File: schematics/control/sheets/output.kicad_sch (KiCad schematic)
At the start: 17 parts, among them U13 NE5532, U14 TL072

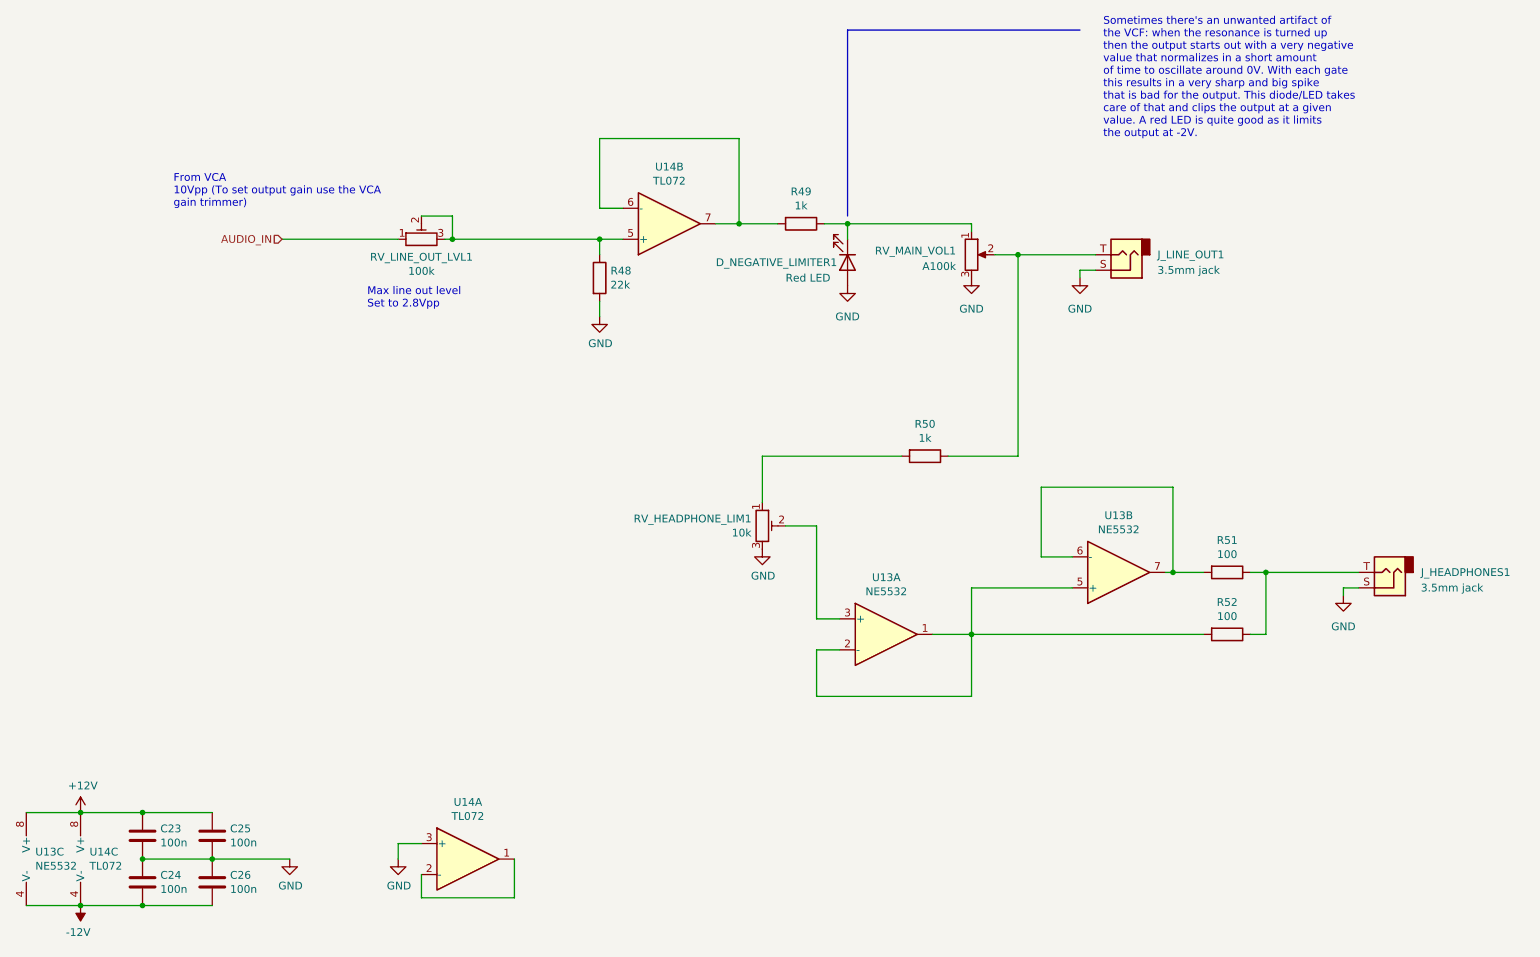
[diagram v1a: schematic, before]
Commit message: Added pulse width mod schematics
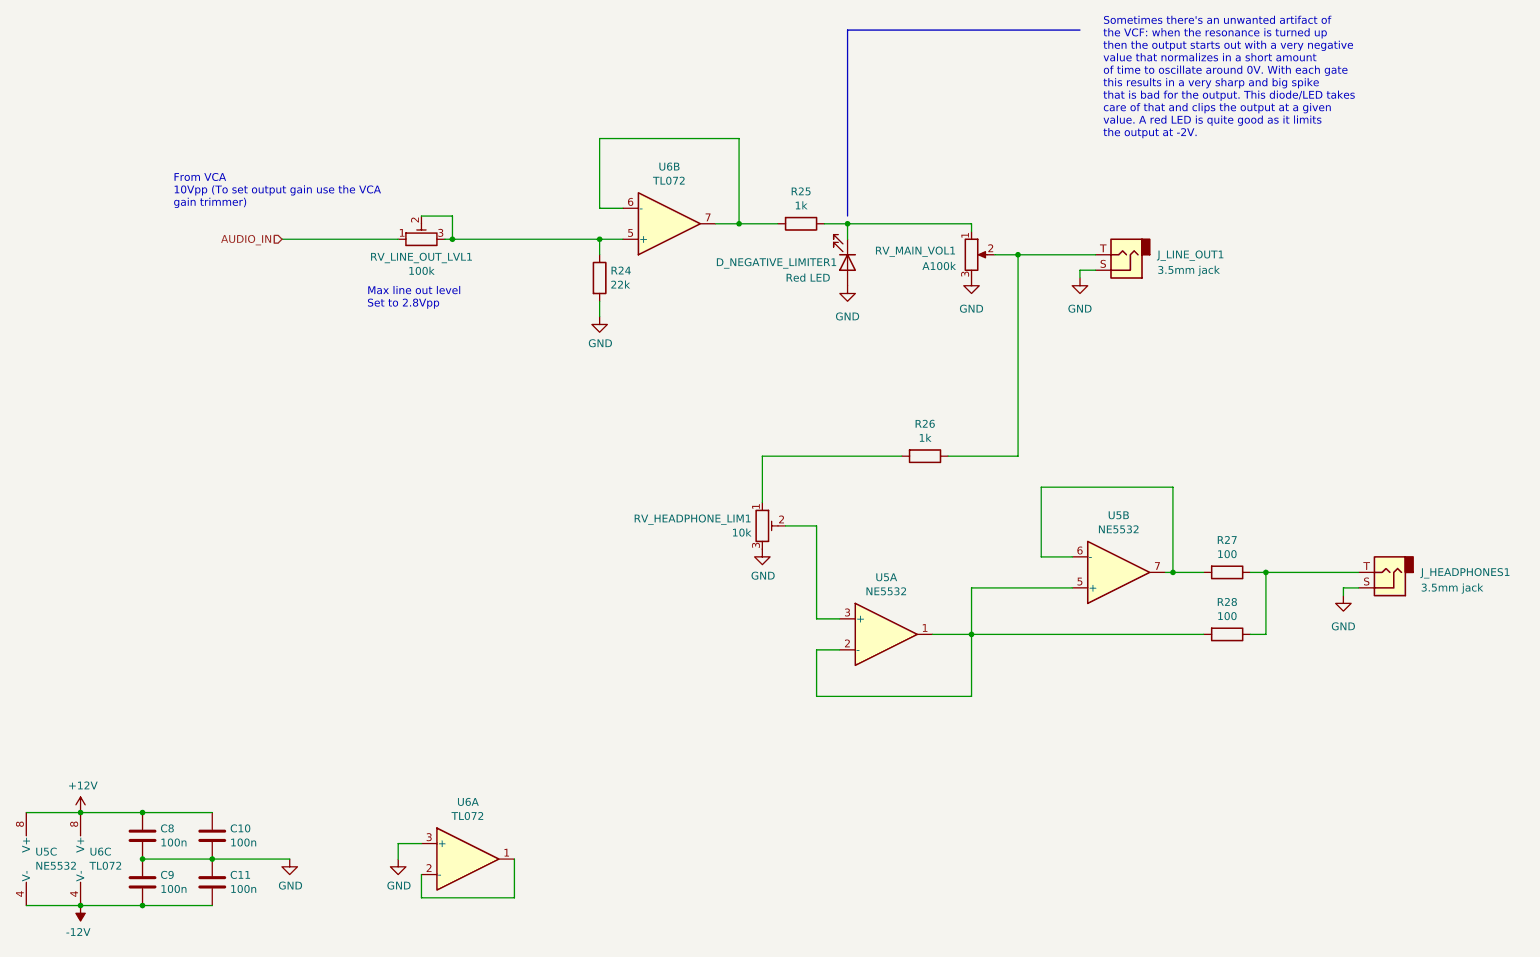
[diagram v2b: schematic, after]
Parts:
- renumbered C25 to C10, C26 to C11, C23 to C8, C24 to C9, R48 to R24, R49 to R25, R50 to R26, R51 to R27, R52 to R28, U13 to U5, U14 to U6

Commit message: Updated VCA
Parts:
- removed unit 1 of U6

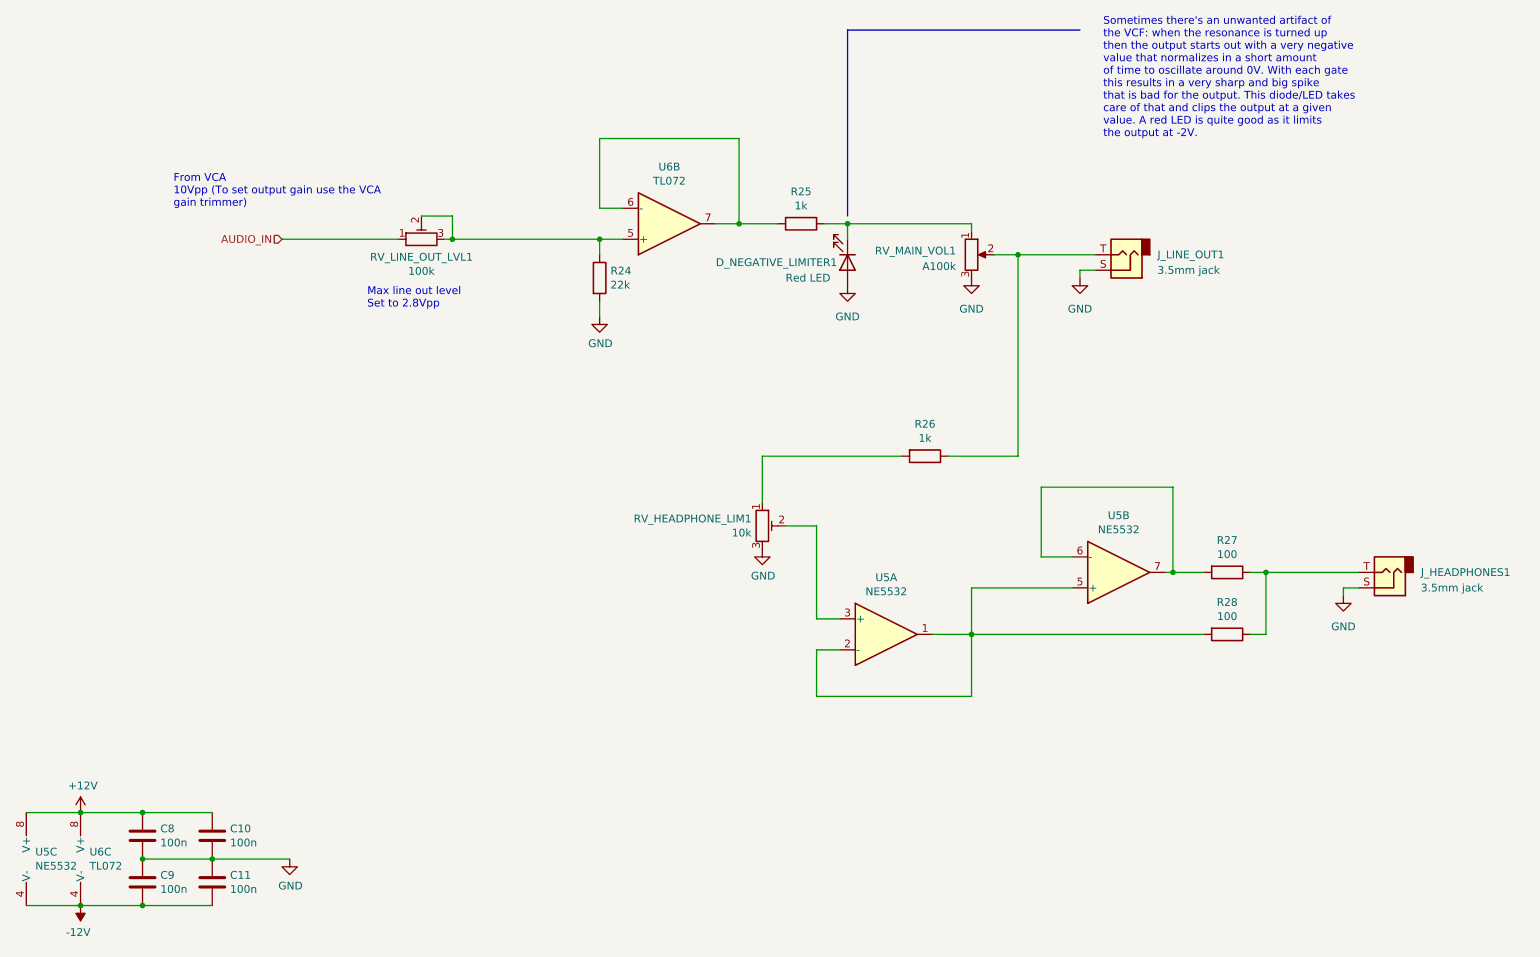
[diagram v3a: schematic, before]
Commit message: Added all UI components to schematics
- digital UI
- filter UI
- updated voice interface connection
- simplified schematics a lot
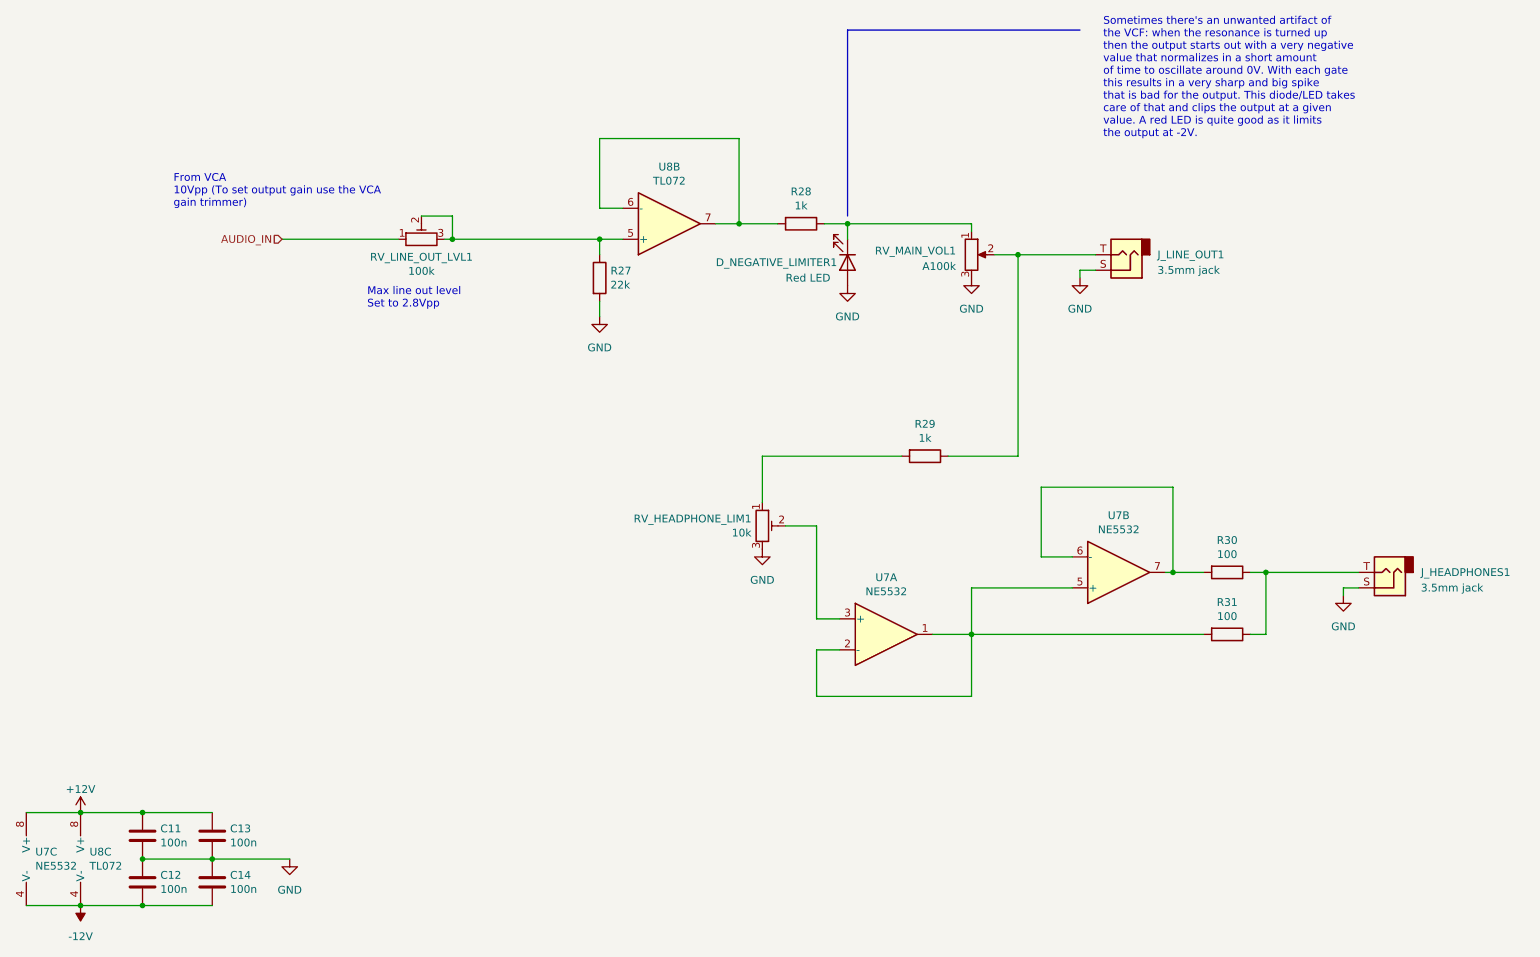
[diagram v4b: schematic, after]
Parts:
- C11: renamed from C8; footprint Capacitor_THT:C_Disc_D3.0mm_W2.0mm_P2.50mm -> (none)
- C12: renamed from C9; footprint Capacitor_THT:C_Disc_D3.0mm_W2.0mm_P2.50mm -> (none)
- C13: renamed from C10; footprint Capacitor_THT:C_Disc_D3.0mm_W2.0mm_P2.50mm -> (none)
- C14: renamed from C11; footprint Capacitor_THT:C_Disc_D3.0mm_W2.0mm_P2.50mm -> (none)
- D_NEGATIVE_LIMITER1: footprint LED_THT:LED_D5.0mm -> (none)
- J_HEADPHONES1, J_LINE_OUT1: footprint Shmoergh_Custom_Footprints:NSL25_01x02_Vertical-AudioJack-TS -> (none)
- R27: renamed from R24; footprint Shmoergh_Custom_Footprints:R_Axial_DIN0207_L6.3mm_D2.5mm_P7.62mm_Horizontal -> (none)
- R28: renamed from R25; footprint Shmoergh_Custom_Footprints:R_Axial_DIN0207_L6.3mm_D2.5mm_P7.62mm_Horizontal -> (none)
- R29: renamed from R26; footprint Shmoergh_Custom_Footprints:R_Axial_DIN0207_L6.3mm_D2.5mm_P7.62mm_Horizontal -> (none)
- R30: renamed from R27; footprint Shmoergh_Custom_Footprints:R_Axial_DIN0207_L6.3mm_D2.5mm_P7.62mm_Horizontal -> (none)
- R31: renamed from R28; footprint Shmoergh_Custom_Footprints:R_Axial_DIN0207_L6.3mm_D2.5mm_P7.62mm_Horizontal -> (none)
- RV_HEADPHONE_LIM1, RV_LINE_OUT_LVL1: footprint Potentiometer_THT:Potentiometer_Runtron_RM-065_Vertical -> (none)
- RV_MAIN_VOL1: footprint Shmoergh_Custom_Footprints:NSL25_01x03_Vertical -> (none)
- U7: renamed from U5; footprint Package_DIP:DIP-8_W7.62mm -> (none)
- U8: renamed from U6; footprint Package_DIP:DIP-8_W7.62mm -> (none)

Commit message: Schemo work
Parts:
- C11, C12, C13, C14: footprint (none) -> Capacitor_THT:C_Disc_D3.0mm_W2.0mm_P2.50mm
- D_NEGATIVE_LIMITER1: footprint (none) -> LED_THT:LED_D5.0mm
- J_HEADPHONES1, J_LINE_OUT1: footprint (none) -> Shmoergh_Custom_Footprints:NSL25_01x02_Vertical-AudioJack-TS
- R27, R28, R29, R30, R31: footprint (none) -> Shmoergh_Custom_Footprints:R_Axial_DIN0207_L6.3mm_D2.5mm_P7.62mm_Horizontal
- RV_HEADPHONE_LIM1, RV_LINE_OUT_LVL1: footprint (none) -> Potentiometer_THT:Potentiometer_Runtron_RM-065_Vertical
- RV_MAIN_VOL1: footprint (none) -> Shmoergh_Custom_Footprints:NSL25_01x03_Vertical
- U7, U8: footprint (none) -> PCM_Package_DIP_AKL:DIP-8_W7.62mm_LongPads

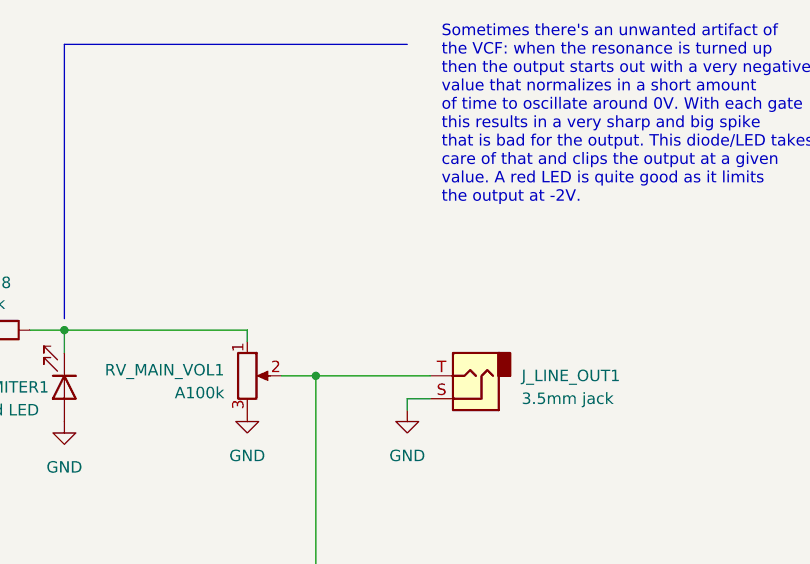
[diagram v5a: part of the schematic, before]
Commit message: Simplified PWM switch IO
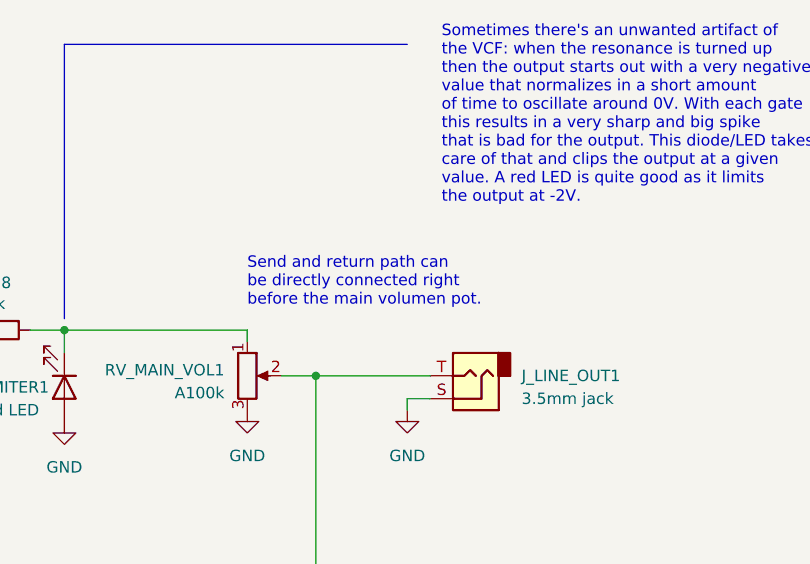
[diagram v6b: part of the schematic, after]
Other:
- note added: "Send and return path can be directly connected right before the main volumen pot."
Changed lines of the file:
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@@
+    (effects (font (size 1.27 1.27)) (justify left bottom))
+  )
+  (text "Send and return path can \nbe directly connected right\nbefore the main volumen pot."
+    (at 179.07 55.88 0)
     (effects (font (size 1.27 1.27)) (justify left bottom))
   )
